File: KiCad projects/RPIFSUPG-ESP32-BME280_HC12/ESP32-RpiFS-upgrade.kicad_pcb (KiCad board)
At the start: 2 copper layers, 29.8 x 49.7 mm, 7 parts, among them J1 HC-12, J2 BME280, U1 ESP32-DEVKITC-32

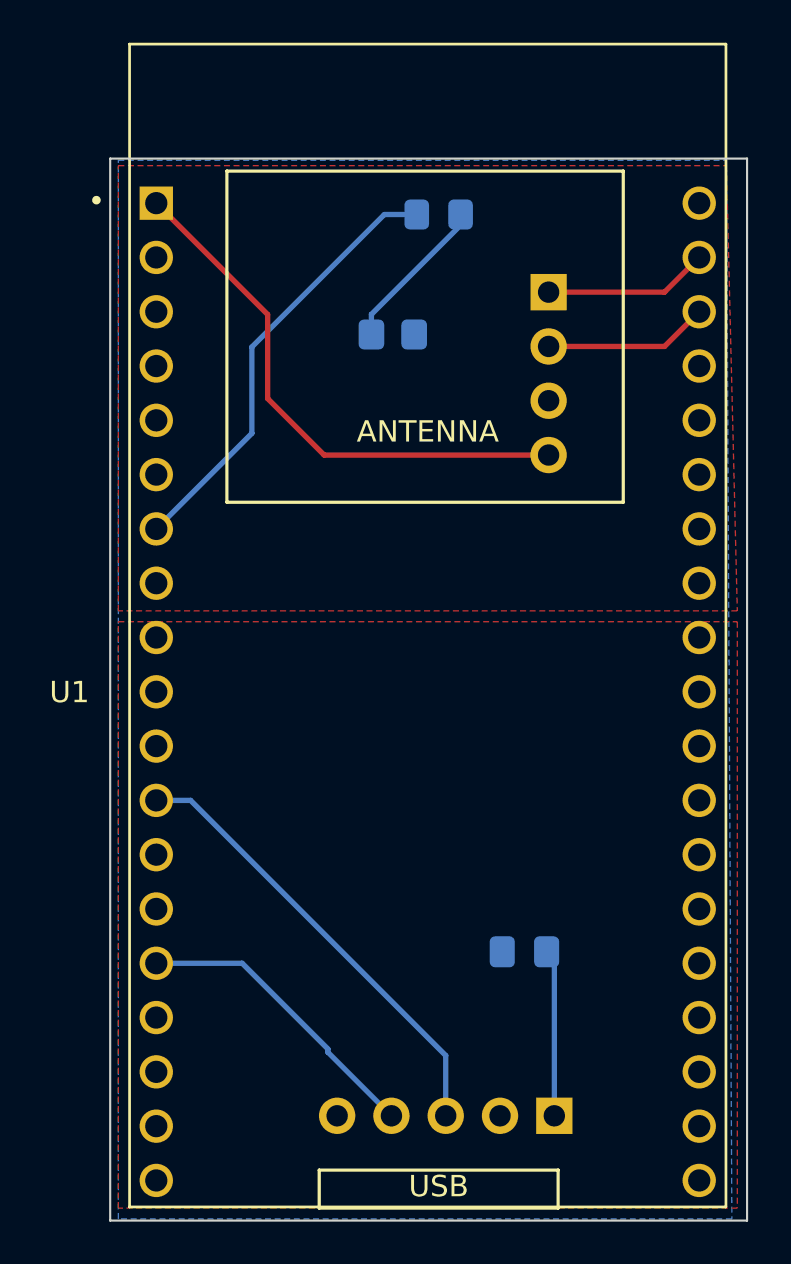
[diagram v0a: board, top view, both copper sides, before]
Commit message: Fixed orientation of headers.
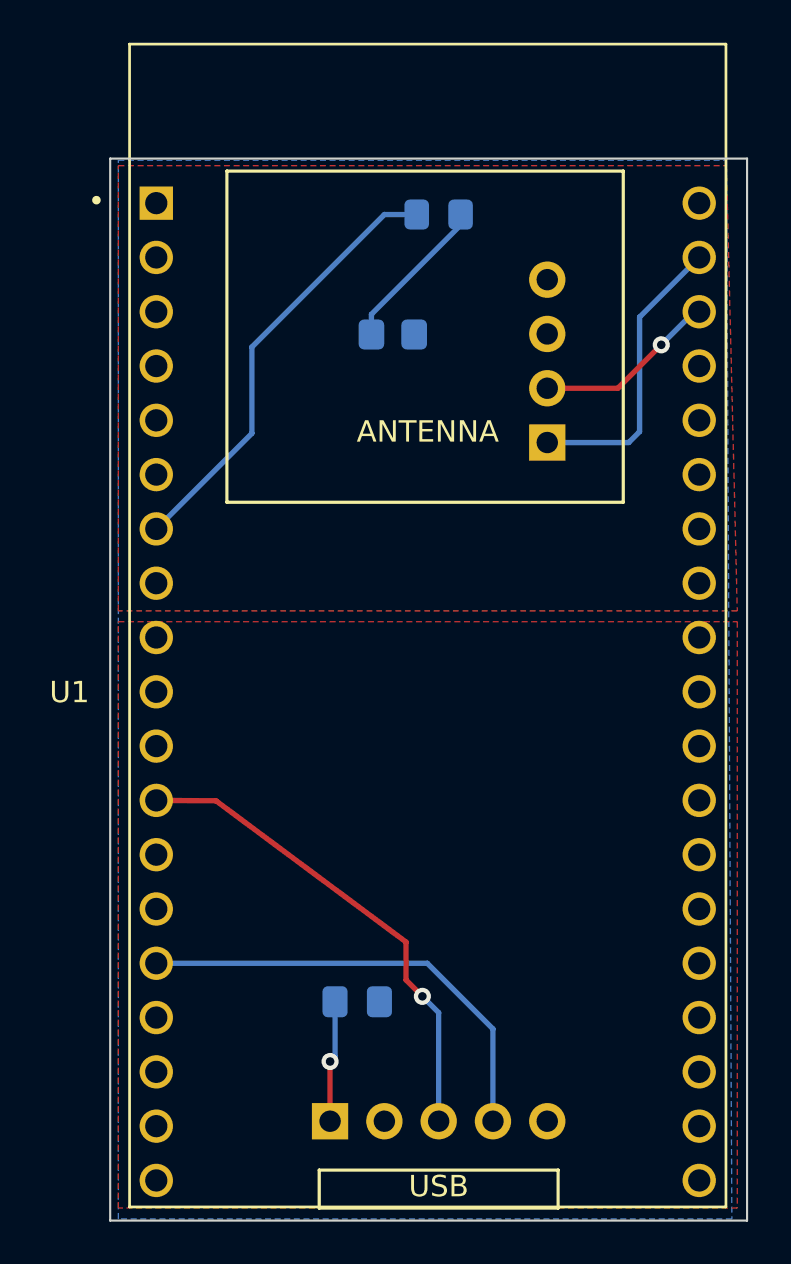
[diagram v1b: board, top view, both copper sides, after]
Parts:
- moved J1 10.5 mm to (141.0, 121.9), turned to -90 degrees
- moved C1 8.16 mm to (142.2, 116.3), turned to 0 degrees
- moved J2 7.04 mm to (151.1, 90.2), turned to 0 degrees
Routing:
- net /Vin: track 25.5 -> 0.00 mm
- net /TXD: track 14.0 -> 21.3 mm
- net /SDA: track 7.72 -> 13.8 mm
- net /VCC: track 7.82 -> 5.68 mm, vias 0 -> 1
- net /RXD: track 21.3 -> 22.9 mm, vias 0 -> 1
- net /SCL: track 7.72 -> 8.59 mm, vias 0 -> 1
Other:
- board text added: "Raspberry Pi Full Stack Upgrade Project Breakout for HC12 & BME280 v2"
- board text removed: "Raspberry Pi Full Stack Upgrade Project Breakout for HC12 & BME280 v1"
